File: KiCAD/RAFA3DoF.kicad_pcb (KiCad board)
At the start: 2 copper layers, 38 x 38 mm, 12 parts, among them IC1 AS5600-ASOT, J1 Conn_01x04, J2 Conn_01x02, J3 Conn_01x03, U1 ESP32-C3_SUPERMINI_SMD

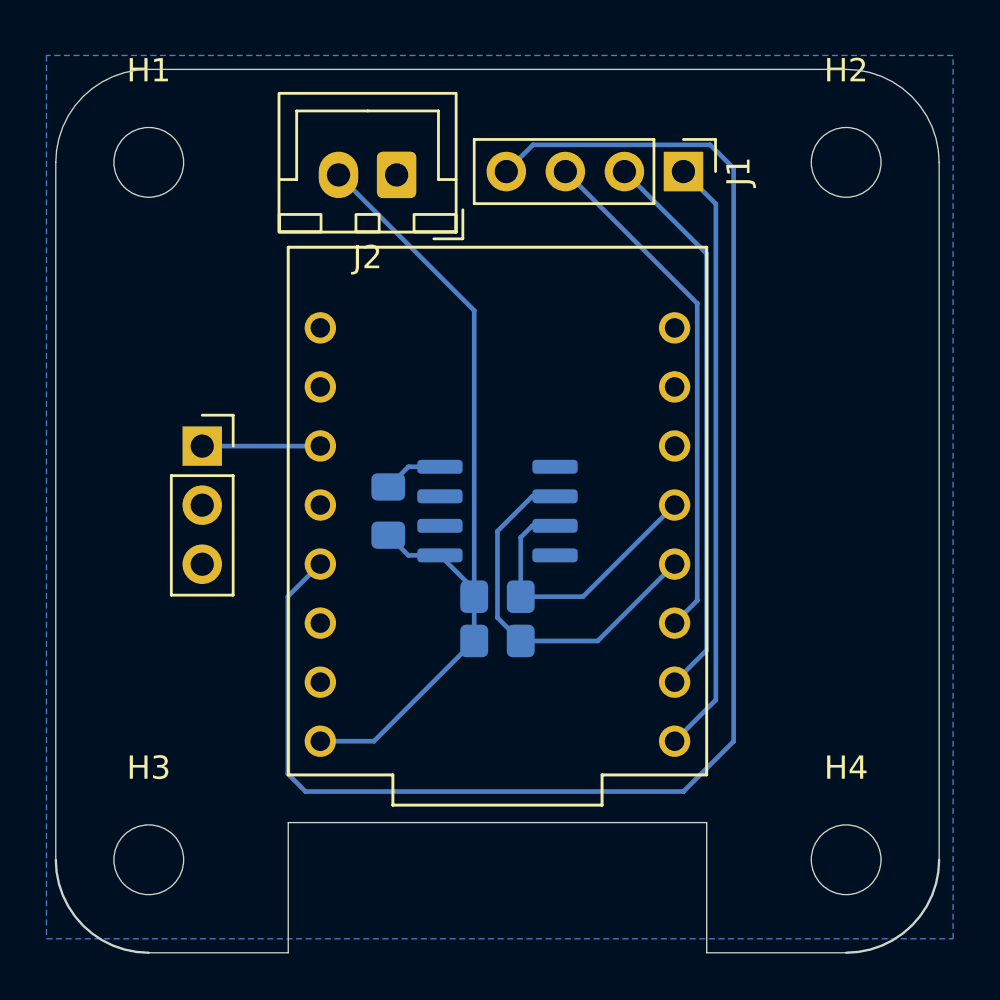
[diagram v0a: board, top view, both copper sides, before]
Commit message: Chenges traces to rounded ones
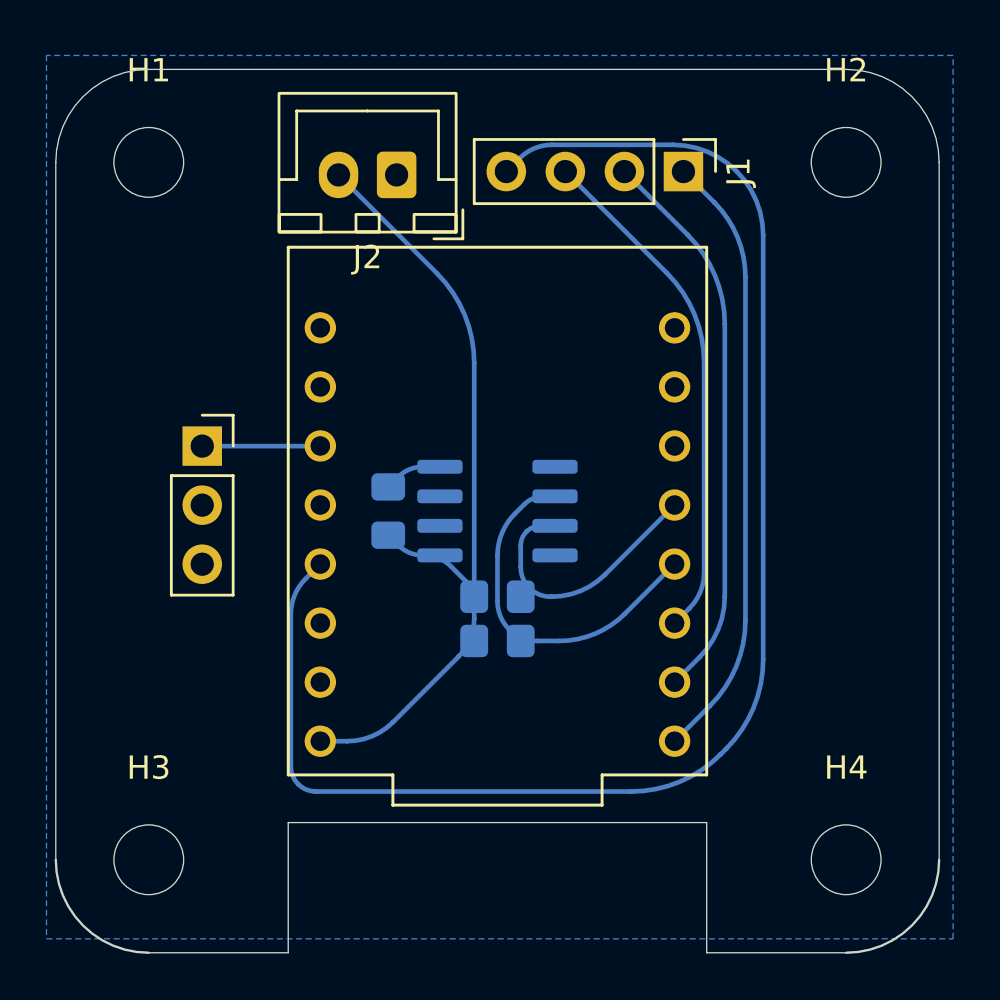
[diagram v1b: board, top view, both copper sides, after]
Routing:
- net /SDA: track 13.1 -> 12.2 mm
- net /MISO: track 25.8 -> 26.4 mm
- net /SCL: track 16.2 -> 15.7 mm
- net 5V: track 35.8 -> 35.3 mm
